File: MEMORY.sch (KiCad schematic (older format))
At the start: 77 parts, among them J901 GND, J902 GND, J903 GND, J904 GND, J905 GND, J906 GND, J907 GND, J908 GND, J909 GND, J910 GND, J911 GND, J912 GND, J913 GND, J914 GND, J915 GND, J916 GND, J917 GND, J918 GND, J919 GND, J920 GND, J921 GND, J922 GND, J923 GND, J924 GND, U801 MCIMX7D7DVM10SC, U901 MT41K256M16HA-125, U902 MT41K256M16HA-125

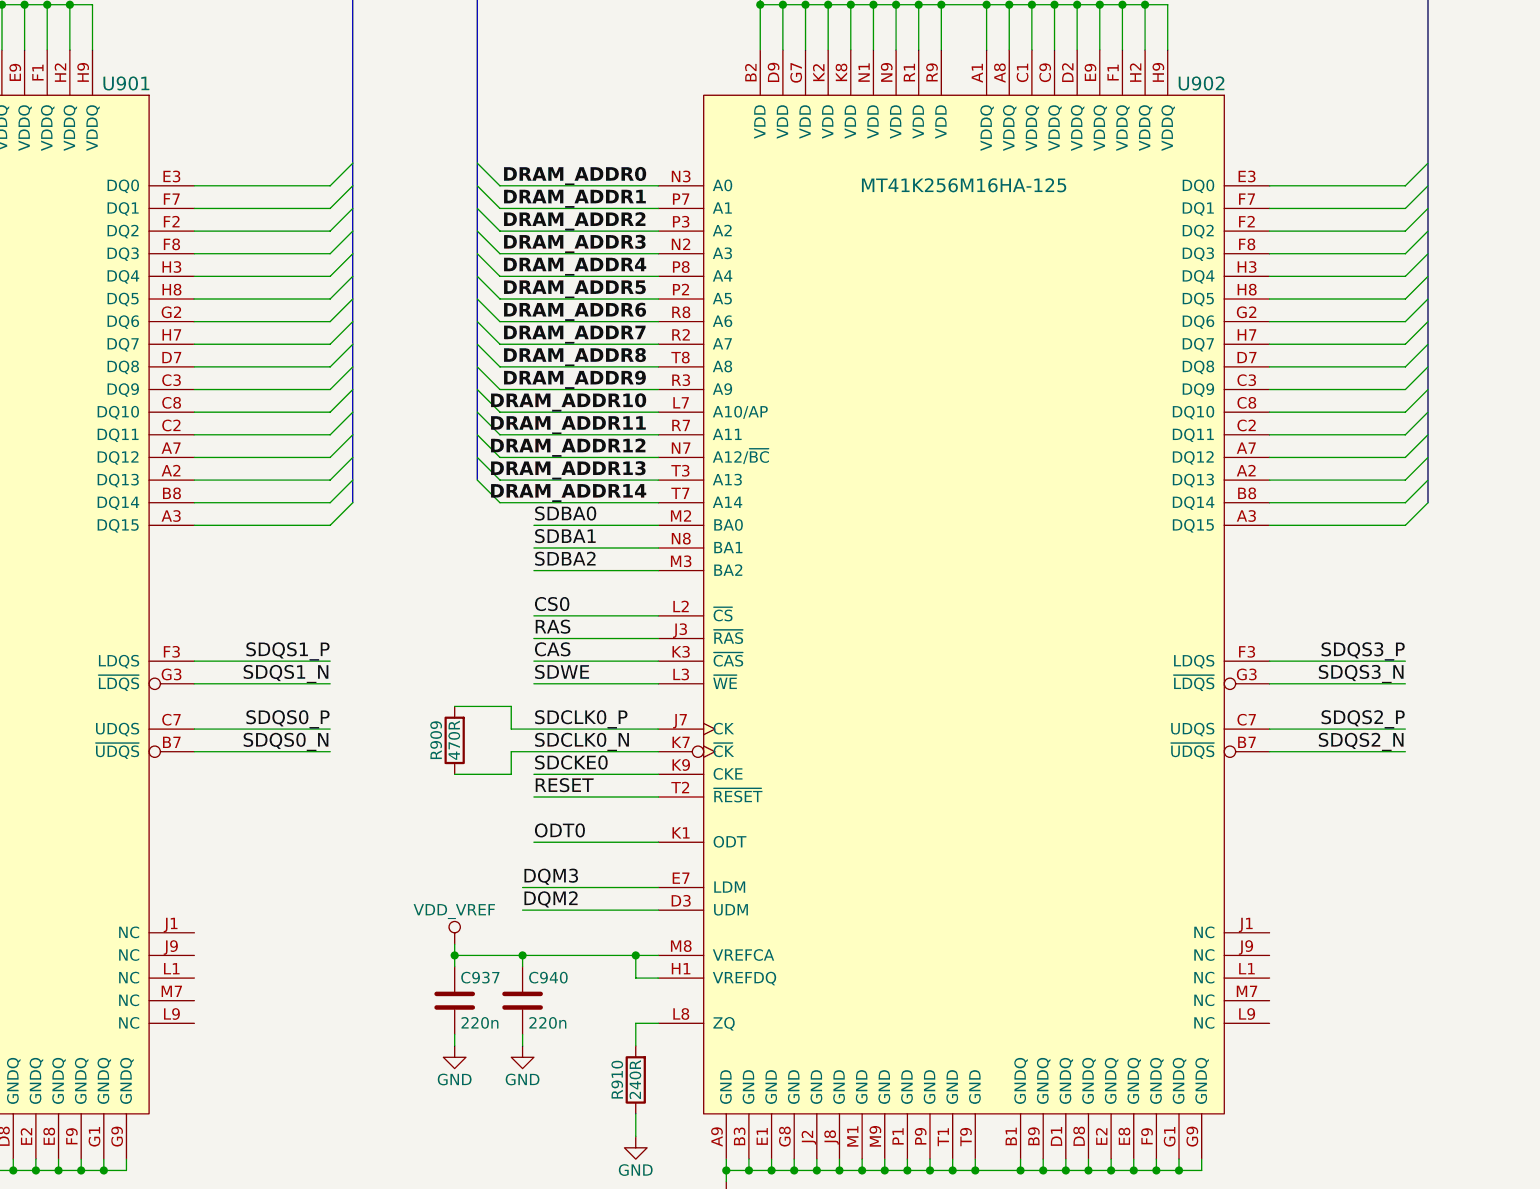
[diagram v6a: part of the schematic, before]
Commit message: Startet routing DDR3. Some things need to be cleared before routign process an begin
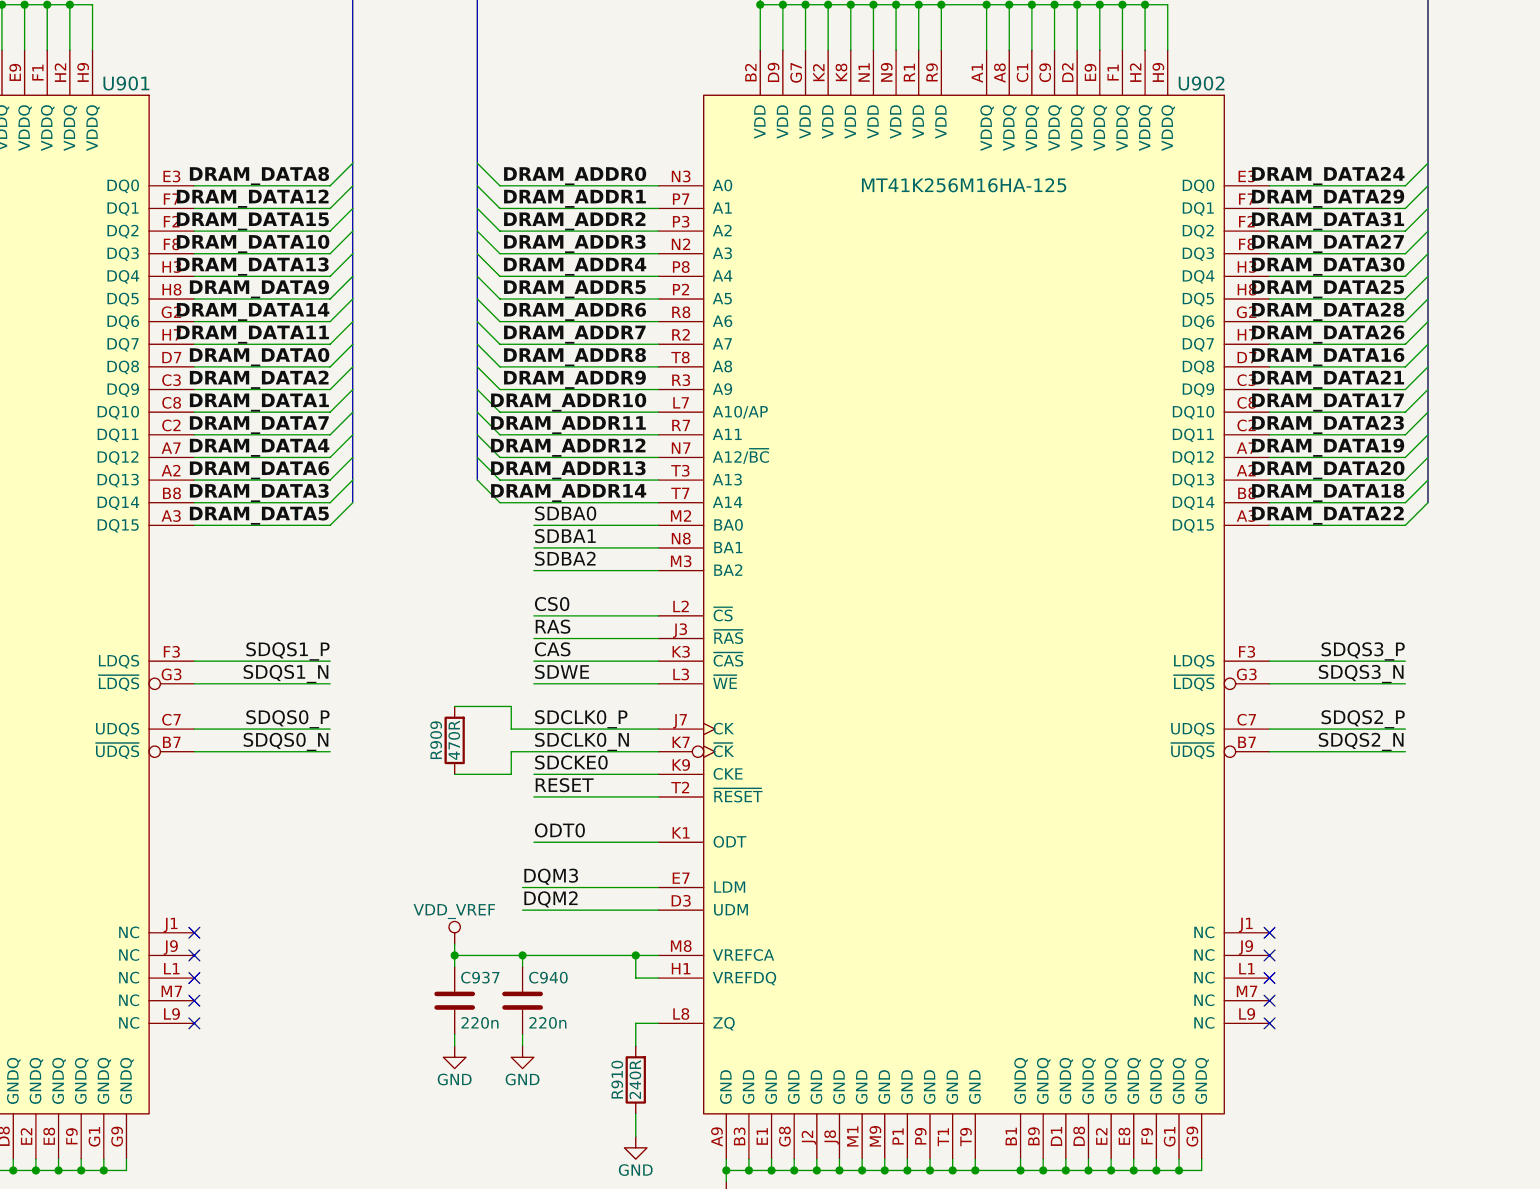
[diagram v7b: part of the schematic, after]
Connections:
- net DRAM_DATA0: now also U901.D7 (DQ8)
- net DRAM_DATA1: now also U901.C8 (DQ10)
- net DRAM_DATA10: now also U901.F8 (DQ3)
- net DRAM_DATA11: now also U901.H7 (DQ7)
- net DRAM_DATA12: now also U901.F7 (DQ1)
- net DRAM_DATA13: now also U901.H3 (DQ4)
- net DRAM_DATA14: now also U901.G2 (DQ6)
- net DRAM_DATA15: now also U901.F2 (DQ2)
- net DRAM_DATA16: now also U902.D7 (DQ8)
- net DRAM_DATA17: now also U902.C8 (DQ10)
- net DRAM_DATA18: now also U902.B8 (DQ14)
- net DRAM_DATA19: now also U902.A7 (DQ12)
- net DRAM_DATA2: now also U901.C3 (DQ9)
- net DRAM_DATA20: now also U902.A2 (DQ13)
- net DRAM_DATA21: now also U902.C3 (DQ9)
- net DRAM_DATA22: now also U902.A3 (DQ15)
- net DRAM_DATA23: now also U902.C2 (DQ11)
- net DRAM_DATA24: now also U902.E3 (DQ0)
- net DRAM_DATA25: now also U902.H8 (DQ5)
- net DRAM_DATA26: now also U902.H7 (DQ7)
- net DRAM_DATA27: now also U902.F8 (DQ3)
- net DRAM_DATA28: now also U902.G2 (DQ6)
- net DRAM_DATA29: now also U902.F7 (DQ1)
- net DRAM_DATA3: now also U901.B8 (DQ14)
- net DRAM_DATA30: now also U902.H3 (DQ4)
- net DRAM_DATA31: now also U902.F2 (DQ2)
- net DRAM_DATA4: now also U901.A7 (DQ12)
- net DRAM_DATA5: now also U901.A3 (DQ15)
- net DRAM_DATA6: now also U901.A2 (DQ13)
- net DRAM_DATA7: now also U901.C2 (DQ11)
- net DRAM_DATA8: now also U901.E3 (DQ0)
- net DRAM_DATA9: now also U901.H8 (DQ5)
- no-connect marks 0 -> 10
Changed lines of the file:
@@
 DQM3
 $Comp
-L NVCC_DRAM #PWR901
+L NVCC_DRAM #PWR0164
 U 1 1 591D8B55
 P 2200 6800
-F 0 "#PWR901" H 2200 6650 50  0001 C CNN
+F 0 "#PWR0164" H 2200 6650 50  0001 C CNN
 F 1 "NVCC_DRAM" H 2200 6950 50  0000 C CNN
 F 2 "" H 2200 6800 50  0001 C CNN
@@
 	6500 7300 6500 7200
 $Comp
-L NVCC_DRAM #PWR911
+L NVCC_DRAM #PWR0165
 U 1 1 591D9FCD
 P 6500 7200
-F 0 "#PWR911" H 6500 7050 50  0001 C CNN
+F 0 "#PWR0165" H 6500 7050 50  0001 C CNN
 F 1 "NVCC_DRAM" H 6500 7350 50  0000 C CNN
 F 2 "" H 6500 7200 50  0001 C CNN
@@
 $EndComp
 $Comp
-L GND #PWR904
+L GND #PWR0166
 U 1 1 591DA1AD
 P 5350 8350
-F 0 "#PWR904" H 5350 8100 50  0001 C CNN
+F 0 "#PWR0166" H 5350 8100 50  0001 C CNN
 F 1 "GND" H 5350 8200 50  0000 C CNN
 F 2 "" H 5350 8350 50  0001 C CNN
@@
 $EndComp
 $Comp
-L GND #PWR905
+L GND #PWR0167
 U 1 1 591DA1D4
 P 5650 8350
-F 0 "#PWR905" H 5650 8100 50  0001 C CNN
+F 0 "#PWR0167" H 5650 8100 50  0001 C CNN
 F 1 "GND" H 5650 8200 50  0000 C CNN
 F 2 "" H 5650 8350 50  0001 C CNN
@@
 $EndComp
 $Comp
-L GND #PWR906
+L GND #PWR0168
 U 1 1 591DA1F4
 P 5950 8350
-F 0 "#PWR906" H 5950 8100 50  0001 C CNN
+F 0 "#PWR0168" H 5950 8100 50  0001 C CNN
 F 1 "GND" H 5950 8200 50  0000 C CNN
 F 2 "" H 5950 8350 50  0001 C CNN
@@
 DQM0
 $Comp
-L VDD_VREF #PWR909
+L VDD_VREF #PWR0169
 U 1 1 591DA9C3
 P 6500 6050
-F 0 "#PWR909" H 6500 5900 50  0001 C CNN
+F 0 "#PWR0169" H 6500 5900 50  0001 C CNN
 F 1 "VDD_VREF" H 6500 6200 50  0000 C CNN
 F 2 "" H 6500 6050 50  0001 C CNN
@@
 Connection ~ 7300 6100
 $Comp
-L GND #PWR910
+L GND #PWR0170
 U 1 1 591DAF04
 P 6500 6500
-F 0 "#PWR910" H 6500 6250 50  0001 C CNN
+F 0 "#PWR0170" H 6500 6250 50  0001 C CNN
 F 1 "GND" H 6500 6350 50  0000 C CNN
 F 2 "" H 6500 6500 50  0001 C CNN
@@
 	6500 6500 6500 6450
 $Comp
-L GND #PWR912
+L GND #PWR0171
 U 1 1 591DAF31
 P 6800 6500
-F 0 "#PWR912" H 6800 6250 50  0001 C CNN
+F 0 "#PWR0171" H 6800 6250 50  0001 C CNN
 F 1 "GND" H 6800 6350 50  0000 C CNN
 F 2 "" H 6800 6500 50  0001 C CNN
@@
 	6800 6500 6800 6450
 $Comp
-L GND #PWR917
+L GND #PWR0172
 U 1 1 591DB057
 P 7300 6900
-F 0 "#PWR917" H 7300 6650 50  0001 C CNN
+F 0 "#PWR0172" H 7300 6650 50  0001 C CNN
 F 1 "GND" H 7300 6750 50  0000 C CNN
 F 2 "" H 7300 6900 50  0001 C CNN
@@
 	7300 6400 7300 6500
 $Comp
-L GND #PWR918
+L GND #PWR0173
 U 1 1 591DB3A1
 P 7700 7100
-F 0 "#PWR918" H 7700 6850 50  0001 C CNN
+F 0 "#PWR0173" H 7700 6850 50  0001 C CNN
 F 1 "GND" H 7700 6950 50  0000 C CNN
 F 2 "" H 7700 7100 50  0001 C CNN
@@
 SDQS2_N
 $Comp
-L GND #PWR927
+L GND #PWR0174
 U 1 1 591DD3B2
 P 12050 6900
-F 0 "#PWR927" H 12050 6650 50  0001 C CNN
+F 0 "#PWR0174" H 12050 6650 50  0001 C CNN
 F 1 "GND" H 12050 6750 50  0000 C CNN
 F 2 "" H 12050 6900 50  0001 C CNN
@@
 $EndComp
 $Comp
-L GND #PWR928
+L GND #PWR0175
 U 1 1 591DD3B8
 P 12450 7100
-F 0 "#PWR928" H 12450 6850 50  0001 C CNN
+F 0 "#PWR0175" H 12450 6850 50  0001 C CNN
 F 1 "GND" H 12450 6950 50  0000 C CNN
 F 2 "" H 12450 7100 50  0001 C CNN
@@
 	12050 6400 12050 6500
 $Comp
-L VDD_VREF #PWR924
+L VDD_VREF #PWR0176
 U 1 1 591DD5A2
 P 11250 6050
-F 0 "#PWR924" H 11250 5900 50  0001 C CNN
+F 0 "#PWR0176" H 11250 5900 50  0001 C CNN
 F 1 "VDD_VREF" H 11250 6200 50  0000 C CNN
 F 2 "" H 11250 6050 50  0001 C CNN
@@
 Connection ~ 11550 6100
 $Comp
-L GND #PWR925
+L GND #PWR0177
 U 1 1 591DD5B9
 P 11250 6500
-F 0 "#PWR925" H 11250 6250 50  0001 C CNN
+F 0 "#PWR0177" H 11250 6250 50  0001 C CNN
 F 1 "GND" H 11250 6350 50  0000 C CNN
 F 2 "" H 11250 6500 50  0001 C CNN
@@
 	11250 6500 11250 6450
 $Comp
-L GND #PWR926
+L GND #PWR0178
 U 1 1 591DD5C0
 P 11550 6500
-F 0 "#PWR926" H 11550 6250 50  0001 C CNN
+F 0 "#PWR0178" H 11550 6250 50  0001 C CNN
 F 1 "GND" H 11550 6350 50  0000 C CNN
 F 2 "" H 11550 6500 50  0001 C CNN
@@
 Connection ~ 8150 1900
 $Comp
-L NVCC_DRAM #PWR929
+L NVCC_DRAM #PWR0179
 U 1 1 591DF650
 P 12600 1850
-F 0 "#PWR929" H 12600 1700 50  0001 C CNN
+F 0 "#PWR0179" H 12600 1700 50  0001 C CNN
 F 1 "NVCC_DRAM" H 12600 2000 50  0000 C CNN
 F 2 "" H 12600 1850 50  0001 C CNN
@@
 	11500 5300 11500 5200
 $Comp
-L GND #PWR908
+L GND #PWR0180
 U 1 1 591E04B8
 P 6000 6900
-F 0 "#PWR908" H 6000 6650 50  0001 C CNN
+F 0 "#PWR0180" H 6000 6650 50  0001 C CNN
 F 1 "GND" H 6000 6750 50  0000 C CNN
 F 2 "" H 6000 6900 50  0001 C CNN
@@
 $EndComp
 $Comp
-L GND #PWR907
+L GND #PWR0181
 U 1 1 591E355B
 P 6000 6100
-F 0 "#PWR907" H 6000 5850 50  0001 C CNN
+F 0 "#PWR0181" H 6000 5850 50  0001 C CNN
 F 1 "GND" H 6000 5950 50  0000 C CNN
 F 2 "" H 6000 6100 50  0001 C CNN
@@
 $EndComp
 $Comp
-L NVCC_DRAM #PWR902
+L NVCC_DRAM #PWR0182
 U 1 1 591E38C2
 P 2900 9400
-F 0 "#PWR902" H 2900 9250 50  0001 C CNN
+F 0 "#PWR0182" H 2900 9250 50  0001 C CNN
 F 1 "NVCC_DRAM" H 2900 9550 50  0000 C CNN
 F 2 "" H 2900 9400 50  0001 C CNN
@@
 	4400 9850 4400 9800
 $Comp
-L GND #PWR903
+L GND #PWR0183
 U 1 1 591E4185
 P 2900 9900
-F 0 "#PWR903" H 2900 9650 50  0001 C CNN
+F 0 "#PWR0183" H 2900 9650 50  0001 C CNN
 F 1 "GND" H 2900 9750 50  0000 C CNN
 F 2 "" H 2900 9900 50  0001 C CNN
@@
 $EndComp
 $Comp
-L NVCC_DRAM #PWR913
+L NVCC_DRAM #PWR0184
 U 1 1 591E46CB
 P 7050 8450
-F 0 "#PWR913" H 7050 8300 50  0001 C CNN
+F 0 "#PWR0184" H 7050 8300 50  0001 C CNN
 F 1 "NVCC_DRAM" H 7050 8600 50  0000 C CNN
 F 2 "" H 7050 8450 50  0001 C CNN
@@
 	8850 8900 8850 8850
 $Comp
-L GND #PWR914
+L GND #PWR0185
 U 1 1 591E46FE
 P 7050 8950
-F 0 "#PWR914" H 7050 8700 50  0001 C CNN
+F 0 "#PWR0185" H 7050 8700 50  0001 C CNN
 F 1 "GND" H 7050 8800 50  0000 C CNN
 F 2 "" H 7050 8950 50  0001 C CNN
@@
 $EndComp
 $Comp
-L NVCC_DRAM #PWR915
+L NVCC_DRAM #PWR0186
 U 1 1 591E4F77
 P 7050 9400
-F 0 "#PWR915" H 7050 9250 50  0001 C CNN
+F 0 "#PWR0186" H 7050 9250 50  0001 C CNN
 F 1 "NVCC_DRAM" H 7050 9550 50  0000 C CNN
 F 2 "" H 7050 9400 50  0001 C CNN
@@
 	8850 9850 8850 9800
 $Comp
-L GND #PWR916
+L GND #PWR0187
 U 1 1 591E4FAA
 P 7050 9900
-F 0 "#PWR916" H 7050 9650 50  0001 C CNN
+F 0 "#PWR0187" H 7050 9650 50  0001 C CNN
 F 1 "GND" H 7050 9750 50  0000 C CNN
 F 2 "" H 7050 9900 50  0001 C CNN
@@
 $EndComp
 $Comp
-L NVCC_DRAM #PWR920
+L NVCC_DRAM #PWR0188
 U 1 1 591E6BFA
 P 9550 8450
-F 0 "#PWR920" H 9550 8300 50  0001 C CNN
+F 0 "#PWR0188" H 9550 8300 50  0001 C CNN
 F 1 "NVCC_DRAM" H 9550 8600 50  0000 C CNN
 F 2 "" H 9550 8450 50  0001 C CNN
@@
 	11350 8900 11350 8850
 $Comp
-L GND #PWR921
+L GND #PWR0189
 U 1 1 591E6C39
 P 9550 8950
-F 0 "#PWR921" H 9550 8700 50  0001 C CNN
+F 0 "#PWR0189" H 9550 8700 50  0001 C CNN
 F 1 "GND" H 9550 8800 50  0000 C CNN
 F 2 "" H 9550 8950 50  0001 C CNN
@@
 $EndComp
 $Comp
-L NVCC_DRAM #PWR922
+L NVCC_DRAM #PWR0190
 U 1 1 591E6C59
 P 9550 9400
-F 0 "#PWR922" H 9550 9250 50  0001 C CNN
+F 0 "#PWR0190" H 9550 9250 50  0001 C CNN
 F 1 "NVCC_DRAM" H 9550 9550 50  0000 C CNN
 F 2 "" H 9550 9400 50  0001 C CNN
@@
 	11350 9850 11350 9800
 $Comp
-L GND #PWR923
+L GND #PWR0191
 U 1 1 591E6C98
 P 9550 9900
-F 0 "#PWR923" H 9550 9650 50  0001 C CNN
+F 0 "#PWR0191" H 9550 9650 50  0001 C CNN
 F 1 "GND" H 9550 9750 50  0000 C CNN
 F 2 "" H 9550 9900 50  0001 C CNN
@@
 	7850 1850 7850 2100
 $Comp
-L NVCC_DRAM #PWR919
+L NVCC_DRAM #PWR0192
 U 1 1 591DDA84
 P 7850 1850
-F 0 "#PWR919" H 7850 1700 50  0001 C CNN
+F 0 "#PWR0192" H 7850 1700 50  0001 C CNN
 F 1 "NVCC_DRAM" H 7850 2000 50  0000 C CNN
 F 2 "" H 7850 1850 50  0001 C CNN
@@
 	1    0    0    -1
 $EndComp
+Text Label 10700 2700 2    60   ~ 12
+DRAM_DATA8
+Text Label 10700 2800 2    60   ~ 12
+DRAM_DATA12
+Text Label 10700 2900 2    60   ~ 12
+DRAM_DATA15
+Text Label 10700 3000 2    60   ~ 12
+DRAM_DATA10
+Text Label 10700 3100 2    60   ~ 12
+DRAM_DATA13
+Text Label 10700 3200 2    60   ~ 12
+DRAM_DATA9
+Text Label 10700 3300 2    60   ~ 12
+DRAM_DATA14
+Text Label 10700 3400 2    60   ~ 12
+DRAM_DATA11
+Text Label 10700 3500 2    60   ~ 12
+DRAM_DATA0
+Text Label 10700 3600 2    60   ~ 12
+DRAM_DATA2
+Text Label 10700 3700 2    60   ~ 12
+DRAM_DATA1
+Text Label 10700 3800 2    60   ~ 12
+DRAM_DATA7
+Text Label 10700 3900 2    60   ~ 12
+DRAM_DATA4
+Text Label 10700 4000 2    60   ~ 12
+DRAM_DATA6
+Text Label 10700 4100 2    60   ~ 12
+DRAM_DATA3
+Text Label 10700 4200 2    60   ~ 12
+DRAM_DATA5
+Text Label 15450 2700 2    60   ~ 12
+DRAM_DATA24
+Text Label 15450 2800 2    60   ~ 12
+DRAM_DATA29
+Text Label 15450 2900 2    60   ~ 12
+DRAM_DATA31
+Text Label 15450 3000 2    60   ~ 12
+DRAM_DATA27
+Text Label 15450 3100 2    60   ~ 12
+DRAM_DATA30
+Text Label 15450 3200 2    60   ~ 12
+DRAM_DATA25
+Text Label 15450 3300 2    60   ~ 12
+DRAM_DATA28
+Text Label 15450 3400 2    60   ~ 12
+DRAM_DATA26
+Text Label 15450 3500 2    60   ~ 12
+DRAM_DATA16
+Text Label 15450 3600 2    60   ~ 12
+DRAM_DATA21
+Text Label 15450 3700 2    60   ~ 12
+DRAM_DATA17
+Text Label 15450 3800 2    60   ~ 12
+DRAM_DATA23
+Text Label 15450 3900 2    60   ~ 12
+DRAM_DATA19
+Text Label 15450 4000 2    60   ~ 12
+DRAM_DATA20
+Text Label 15450 4100 2    60   ~ 12
+DRAM_DATA18
+Text Label 15450 4200 2    60   ~ 12
+DRAM_DATA22
+NoConn ~ 10100 6400
+NoConn ~ 10100 6300
+NoConn ~ 10100 6200
+NoConn ~ 10100 6100
+NoConn ~ 10100 6000
+NoConn ~ 14850 6000
+NoConn ~ 14850 6100
+NoConn ~ 14850 6200
+NoConn ~ 14850 6300
+NoConn ~ 14850 6400
 $EndSCHEMATC
